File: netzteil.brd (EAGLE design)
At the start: 50 x 80 mm, 49 parts, among them X1 NEB21R

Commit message: version 2
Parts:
- removed U$4, U$5: SIA440DJ, teile:SC70-6L
- removed U$6, U$7: STL100NH3LL, teile:PG-TDSON-8
- added C17(OPT): 470n, resistor:C0805K
- added C18: 100µ, resistor:153CLV-0605
- added C18(OPT): 100p, resistor:C0805K
- added D1, D2: (no value), diode:SOD323-R
- added M1, M2: STL100NH3LL, teile:PG-TDSON-8
- added R19: 4R7, resistor:M0805
- added R20, R21(/OPT): 0, resistor:M0805
- C16: value 100µ -> 470µ; device resistor:153CLV-0807 -> resistor:153CLV-1010
- D3, D4: value CGRM4001-G -> (none); device diode:SOD-123_MINI-SMA -> diode:SOD323-R
- R1, R2, R3: device resistor-shunt:BVS -> resistor:R2512
- R16: value 0 -> 51
- moved R9 13.4 mm to (46.1, 23.4), turned to 90 degrees
- moved R11 4.93 mm to (37.9, 14.9)
- moved R12 4.33 mm to (34.4, 16.6)
- moved C11 3.10 mm to (47.4, 30.0), turned to 90 degrees
- moved R8 3.07 mm to (45.7, 51.3), turned to 180 degrees
- moved C14 2.59 mm to (29.2, 56.4)
- moved SV2 2.54 mm to (40.6, 16.5)
- moved R5 2.17 mm to (45.7, 47.1), turned to 0 degrees
- moved C13 2.16 mm to (44.1, 18.3), turned to 0 degrees
- moved R1 2.00 mm to (10.7, 43.8)
- moved R18 1.93 mm to (37.2, 17.5)
- moved R10 1.81 mm to (46.1, 16.4)
- moved C5 1.40 mm to (10.8, 23.6)
- moved R6 1.28 mm to (45.7, 49.4), turned to 0 degrees
- moved C6 1.14 mm to (10.8, 25.9)
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- renumbered U$2 to M4, U$3 to M3
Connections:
- new net CLKOUT: U$1.33
- new net GNDA: C11.2, C12.2, C18(OPT).2, LED1.C, R10.1, R12.1, R18.1, R21(/OPT).1, R7.1, R8.1, R9.1, SV1.1, U$1.29, U$1.30, U$1.EXP@1
- new net N$10: C17(OPT).1, R20.1, U$1.25
- new net N$9: C8.1, R19.1, U$1.12
- new net SYNC: R21(/OPT).2, U$1.34
- net +12V: now also C17(OPT).2
- net BG1: now also M2.4; no longer U$5.3, U$7.4
- net GND: now also C18.-; no longer C11.2, C12.2, LED1.C, R10.1, R12.1, R18.1, R7.1, R8.1, R9.1, SV1.1, U$1.29, U$1.30, U$1.34, U$1.EXP@1
- net ISP: now also D2.C, R20.2; no longer U$1.25
- net N$8: now also C18(OPT).1
- net SNSP: now also D1.A, M2.1, M2.2, M2.3; no longer U$5.4, U$5.P$2, U$7.1, U$7.2, U$7.3
- net SW1: now also D1.C, M1.1, M1.2, M1.3, M2.5, M2.6, M2.7, M2.8, M2.TH; no longer U$4.4, U$4.P$2, U$5.1, U$5.2, U$5.5, U$5.6, U$5.P$1, U$6.1, U$6.2, U$6.3, U$7.5, U$7.6, U$7.7, U$7.8, U$7.TH
- net SW2: now also D2.A
- net TG1: now also M1.4; no longer U$4.3, U$6.4
- net VINN: now also C18.+, M1.5, M1.6, M1.7, M1.8, M1.TH, R19.2; no longer C8.1, U$1.12, U$4.1, U$4.2, U$4.5, U$4.6, U$4.P$1, U$6.5, U$6.6, U$6.7, U$6.8, U$6.TH
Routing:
- net VINN: track 68.6 -> 24.2 mm
- net N$9: track 0.00 -> 31.9 mm
- net BG2: track 17.9 -> 39.6 mm
- net N$10: track 0.00 -> 17.3 mm
- net ISP: track 18.9 -> 5.18 mm, vias 2 -> 0
- net +12V: track 74.4 -> 61.0 mm, vias 5 -> 4
- net GND: track 20.3 -> 7.22 mm, vias 35 -> 24
- net GNDA: track 0.00 -> 12.0 mm, vias 0 -> 1
- net SW1: track 38.2 -> 27.6 mm
- net N$24: track 17.0 -> 7.35 mm
- net SYNC: track 0.00 -> 9.57 mm, vias 0 -> 1
- net TG2: track 19.9 -> 28.1 mm
- net N$18: track 17.3 -> 25.3 mm
- net N$14: track 28.8 -> 35.6 mm
- net N$1: track 40.4 -> 46.5 mm
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- added copper zone on layer 1, net GNDA
- removed copper zone on layer 1, net BST2
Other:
- outline, holes or cut-outs redrawn

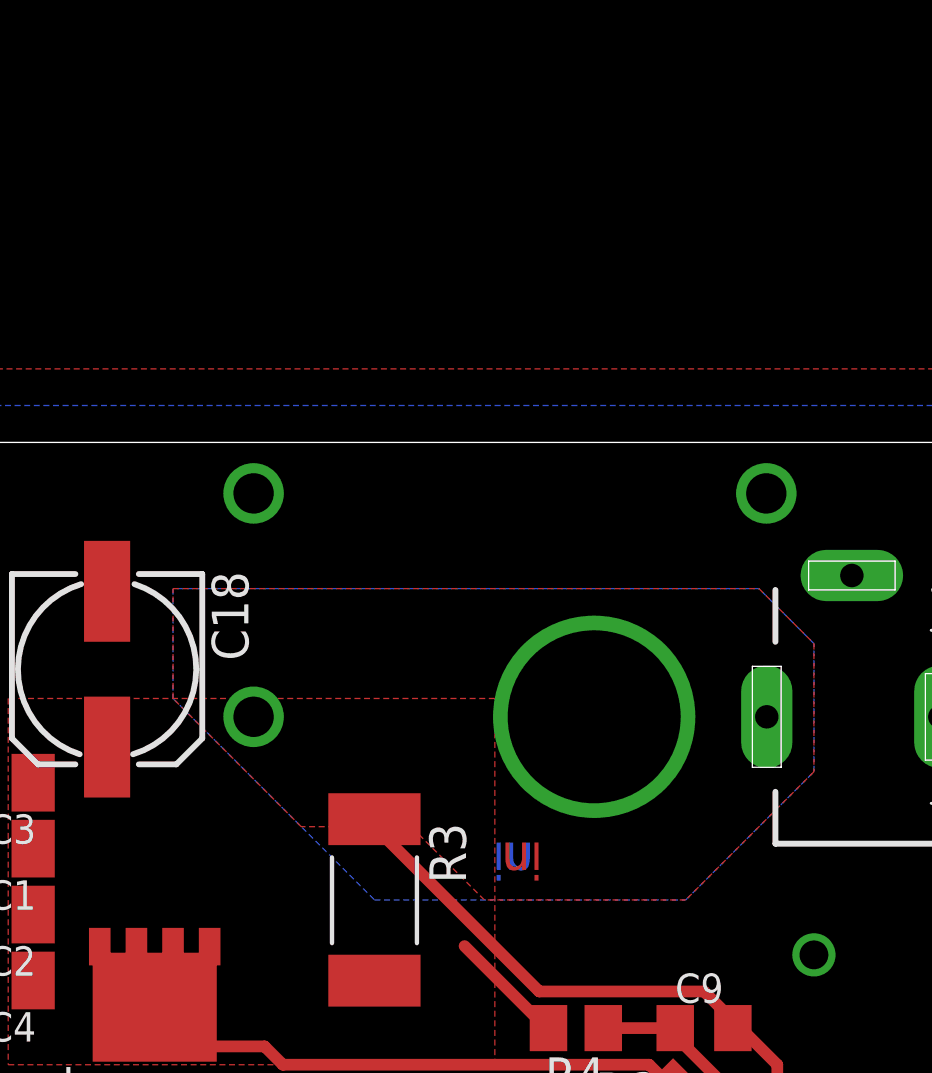
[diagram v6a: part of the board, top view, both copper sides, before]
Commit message: akkustecker
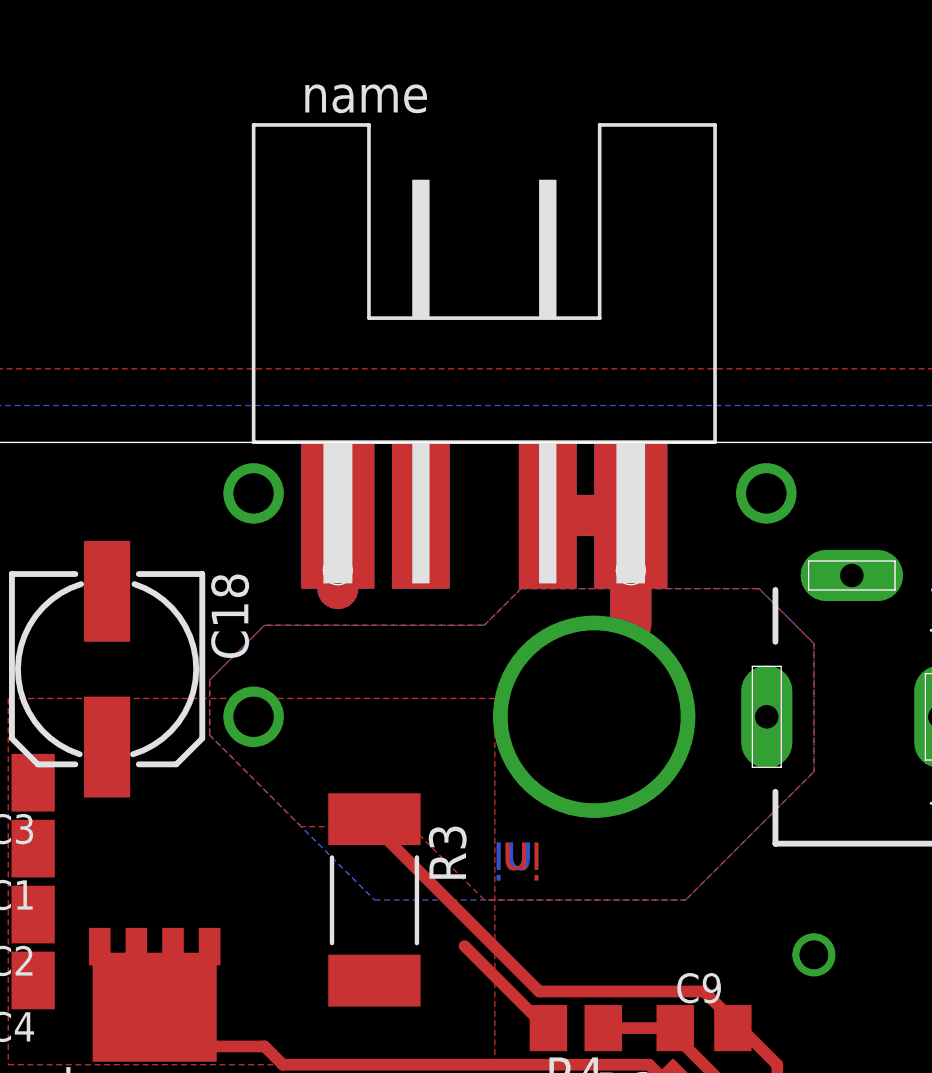
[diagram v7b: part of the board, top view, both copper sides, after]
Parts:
- added U$2: MPX6P, con-ml:MPX6
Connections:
- net +24V: now also U$2.P1A, U$2.P1B, U$2.P2, U$2.P3
- net GND: now also U$2.P4, U$2.P5, U$2.P6A, U$2.P6B
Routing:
- net +24V: track 56.1 -> 69.1 mm
- net GND: track 7.22 -> 12.3 mm
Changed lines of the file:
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@@
 <setting verticaltext="up"/>
 </settings>
-<grid distance="0.05" unitdist="inch" unit="inch" style="lines" multiple="1" display="yes" altdistance="5" altunitdist="mil" altunit="mil"/>
+<grid distance="0.05" unitdist="inch" unit="inch" style="lines" multiple="1" display="yes" altdistance="25" altunitdist="mil" altunit="mil"/>
 <layers>
 <layer number="1" name="Top" color="4" fill="1" visible="yes" active="yes"/>
@@
 <element name="R21(/OPT)" library="resistor" package="M0805" value="0" x="37.211" y="19.431"/>
 <element name="C18" library="resistor" package="153CLV-0605" value="100µ" x="14.859" y="72.136" rot="R270"/>
+<element name="U$2" library="con-ml" package="MPX6" value="MPX6P" x="27.94" y="80.01"/>
 </elements>
 <signals>
@@
 <contactref element="R5" pad="2"/>
 <polygon width="0.4064" layer="1" isolate="0.254">
-<vertex x="17.145" y="74.93"/>
+<vertex x="18.415" y="71.755"/>
+<vertex x="20.32" y="73.66"/>
+<vertex x="27.94" y="73.66"/>
+<vertex x="29.21" y="74.93"/>
 <vertex x="37.465" y="74.93"/>
 <vertex x="39.37" y="73.025"/>
@@
 <vertex x="25.4" y="66.675"/>
 <vertex x="21.59" y="66.675"/>
-<vertex x="17.145" y="71.12"/>
+<vertex x="18.415" y="69.85"/>
 </polygon>
 <wire x1="38.1" y1="58.42" x2="38.1" y2="46.99" width="0.4064" layer="1"/>
@@
 <via x="19.939" y="70.485" extent="1-16" drill="1.4"/>
 <polygon width="0.4064" layer="16" isolate="0.254">
-<vertex x="17.145" y="74.93"/>
-<vertex x="17.145" y="71.12"/>
+<vertex x="18.415" y="71.755"/>
+<vertex x="18.415" y="69.85"/>
 <vertex x="24.13" y="64.135"/>
 <vertex x="34.925" y="64.135"/>
@@
 <vertex x="39.37" y="73.025"/>
 <vertex x="37.465" y="74.93"/>
+<vertex x="29.21" y="74.93"/>
+<vertex x="27.94" y="73.66"/>
+<vertex x="20.32" y="73.66"/>
 </polygon>
 <wire x1="40.64" y1="46.99" x2="41.91" y2="46.99" width="0.4064" layer="1"/>
@@
 <wire x1="46.609" y1="48.26" x2="46.609" y2="49.342" width="0.3048" layer="1"/>
 <wire x1="46.609" y1="49.342" x2="46.67" y2="49.403" width="0.3048" layer="1"/>
+<contactref element="U$2" pad="P2"/>
+<contactref element="U$2" pad="P1A"/>
+<contactref element="U$2" pad="P1B"/>
+<contactref element="U$2" pad="P3"/>
+<wire x1="30.14" y1="77.47" x2="33.02" y2="77.47" width="1.4224" layer="16"/>
+<wire x1="30.48" y1="77.47" x2="33.02" y2="77.47" width="1.4224" layer="1"/>
+<wire x1="33.02" y1="77.47" x2="33.02" y2="73.66" width="1.4224" layer="1"/>
+<wire x1="33.02" y1="73.66" x2="33.02" y2="77.47" width="1.4224" layer="16"/>
 </signal>
 <signal name="VINN">
@@
 <contactref element="X1" pad="2"/>
 <contactref element="C18" pad="-"/>
+<contactref element="U$2" pad="P4"/>
+<contactref element="U$2" pad="P6B"/>
+<contactref element="U$2" pad="P6A"/>
+<contactref element="U$2" pad="P5"/>
+<wire x1="22.86" y1="74.93" x2="22.86" y2="77.47" width="1.4224" layer="1"/>
+<wire x1="22.86" y1="74.93" x2="22.86" y2="77.47" width="1.4224" layer="16"/>
+<wire x1="2.54" y1="11.43" x2="8.255" y2="6.35" width="0" layer="19" extent="1-1"/>
 </signal>
 <signal name="N$12">

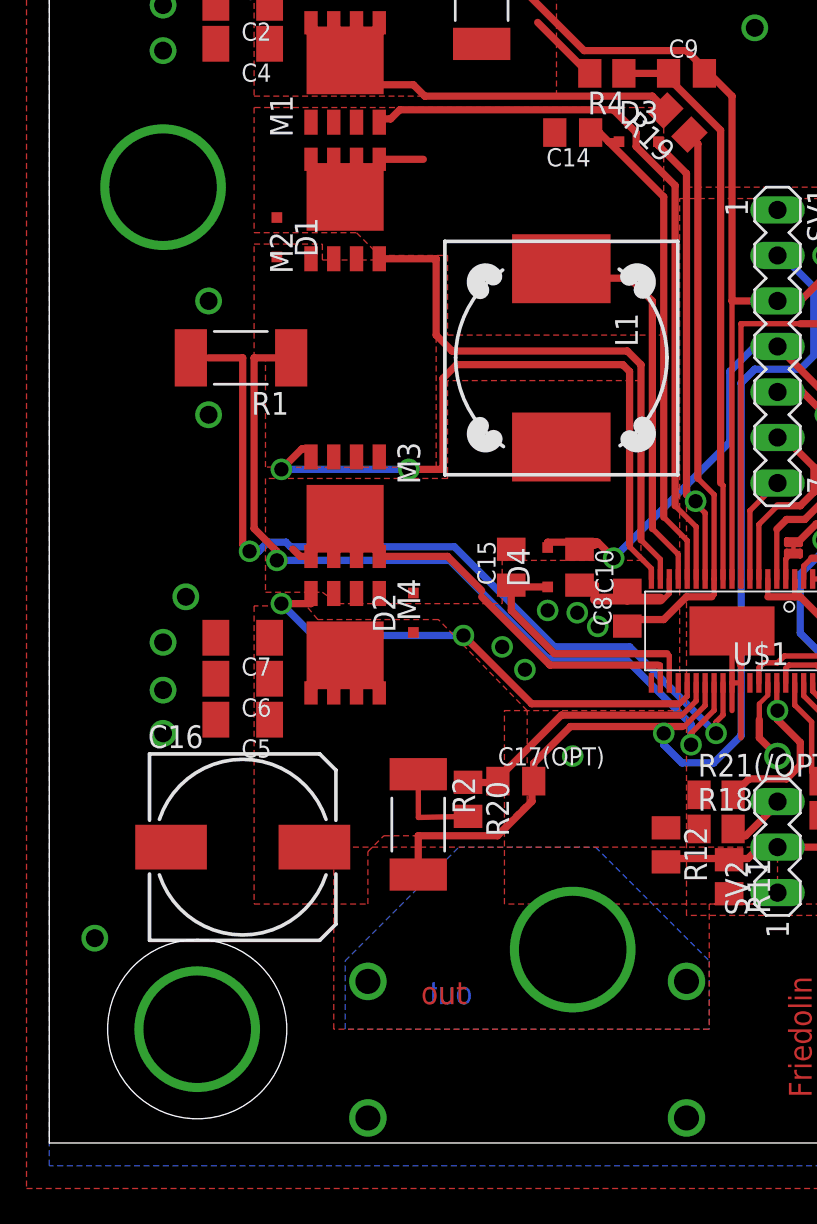
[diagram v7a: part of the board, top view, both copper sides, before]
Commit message: polygon corrections, document layer for circles
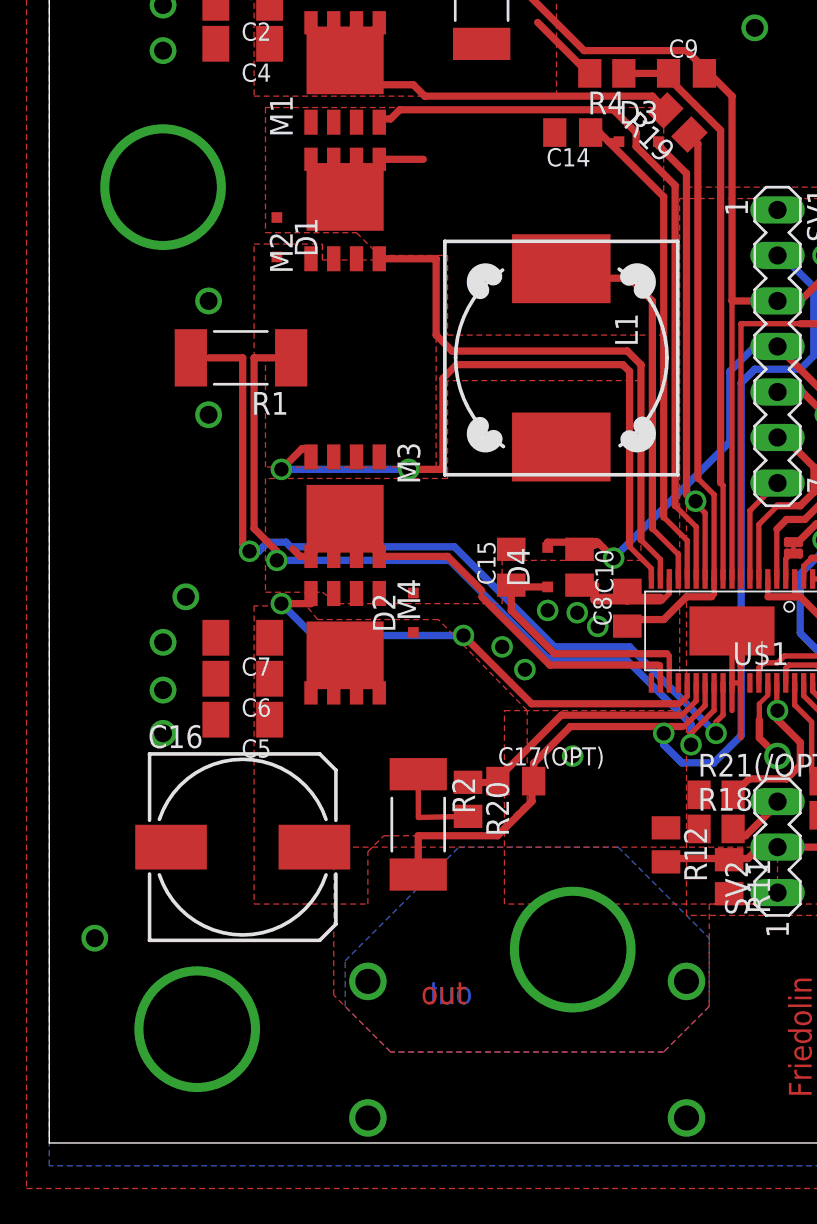
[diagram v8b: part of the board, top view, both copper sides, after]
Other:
- outline, holes or cut-outs redrawn
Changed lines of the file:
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@@
 <layer number="46" name="Milling" color="3" fill="1" visible="no" active="yes"/>
 <layer number="47" name="Measures" color="7" fill="1" visible="no" active="yes"/>
-<layer number="48" name="Document" color="7" fill="1" visible="no" active="yes"/>
+<layer number="48" name="Document" color="7" fill="1" visible="yes" active="yes"/>
 <layer number="49" name="Reference" color="7" fill="1" visible="yes" active="yes"/>
 <layer number="51" name="tDocu" color="7" fill="1" visible="yes" active="yes"/>
@@
 Gröger</text>
 <text x="46.355" y="53.975" size="1.27" layer="1" font="vector" ratio="20" rot="R90">BuckBooster</text>
-<circle x="8.255" y="6.35" radius="5" width="0.01" layer="20"/>
+<circle x="8.255" y="6.35" radius="5" width="0.01" layer="48"/>
+<circle x="29.21" y="10.795" radius="5" width="0.01" layer="48"/>
+<circle x="31.75" y="70.485" radius="5" width="0.01" layer="48"/>
+<circle x="6.35" y="53.34" radius="5" width="0.01" layer="48"/>
 </plain>
 <attributes>
@@
 <vertex x="34.29" y="45.085"/>
 <vertex x="34.29" y="57.785"/>
-<vertex x="11.43" y="57.785"/>
-<vertex x="11.43" y="50.8"/>
+<vertex x="12.065" y="57.785"/>
+<vertex x="12.065" y="50.8"/>
 <vertex x="17.145" y="50.8"/>
 <vertex x="18.415" y="49.53"/>
@@
 <vertex x="40.64" y="13.335"/>
 <vertex x="36.83" y="13.335"/>
-<vertex x="36.83" y="6.35"/>
-<vertex x="15.875" y="6.35"/>
+<vertex x="36.83" y="7.62"/>
+<vertex x="34.29" y="5.08"/>
+<vertex x="19.05" y="5.08"/>
+<vertex x="15.875" y="8.255"/>
 </polygon>
 <wire x1="34.417" y1="23.241" x2="29.083" y2="23.241" width="0.4064" layer="1"/>
@@
 <via x="35.56" y="9.017" extent="1-16" drill="1.4"/>
 <polygon width="0.4064" layer="16" isolate="0.254">
-<vertex x="16.51" y="6.35"/>
+<vertex x="16.51" y="7.62"/>
 <vertex x="16.51" y="10.16"/>
 <vertex x="22.86" y="16.51"/>
-<vertex x="30.48" y="16.51"/>
-<vertex x="36.83" y="10.16"/>
-<vertex x="36.83" y="6.35"/>
+<vertex x="31.75" y="16.51"/>
+<vertex x="36.83" y="11.43"/>
+<vertex x="36.83" y="7.62"/>
+<vertex x="34.29" y="5.08"/>
+<vertex x="19.05" y="5.08"/>
 </polygon>
 <contactref element="SV2" pad="1"/>
@@
 <wire x1="22.86" y1="74.93" x2="22.86" y2="77.47" width="1.4224" layer="1"/>
 <wire x1="22.86" y1="74.93" x2="22.86" y2="77.47" width="1.4224" layer="16"/>
-<wire x1="2.54" y1="11.43" x2="8.255" y2="6.35" width="0" layer="19" extent="1-1"/>
 </signal>
 <signal name="N$12">
